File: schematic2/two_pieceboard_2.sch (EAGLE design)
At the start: 17 parts, among them J1 2X5P-2.54, Q1 MOSFET-NCHANNELFDD8580, Q2 MOSFET-NCHANNELFDD8580, Q4 MOSFET-NCHANNELFDD8580, Q5 MOSFET-NCHANNELFDD8580, Q6 MOSFET-NCHANNELFDD8580, Q7 MOSFET-NCHANNELFDD8580, U3 LM317DCY, X1 MKDSN1,5/2-5,08, X2 MKDSN1,5/3-5,08

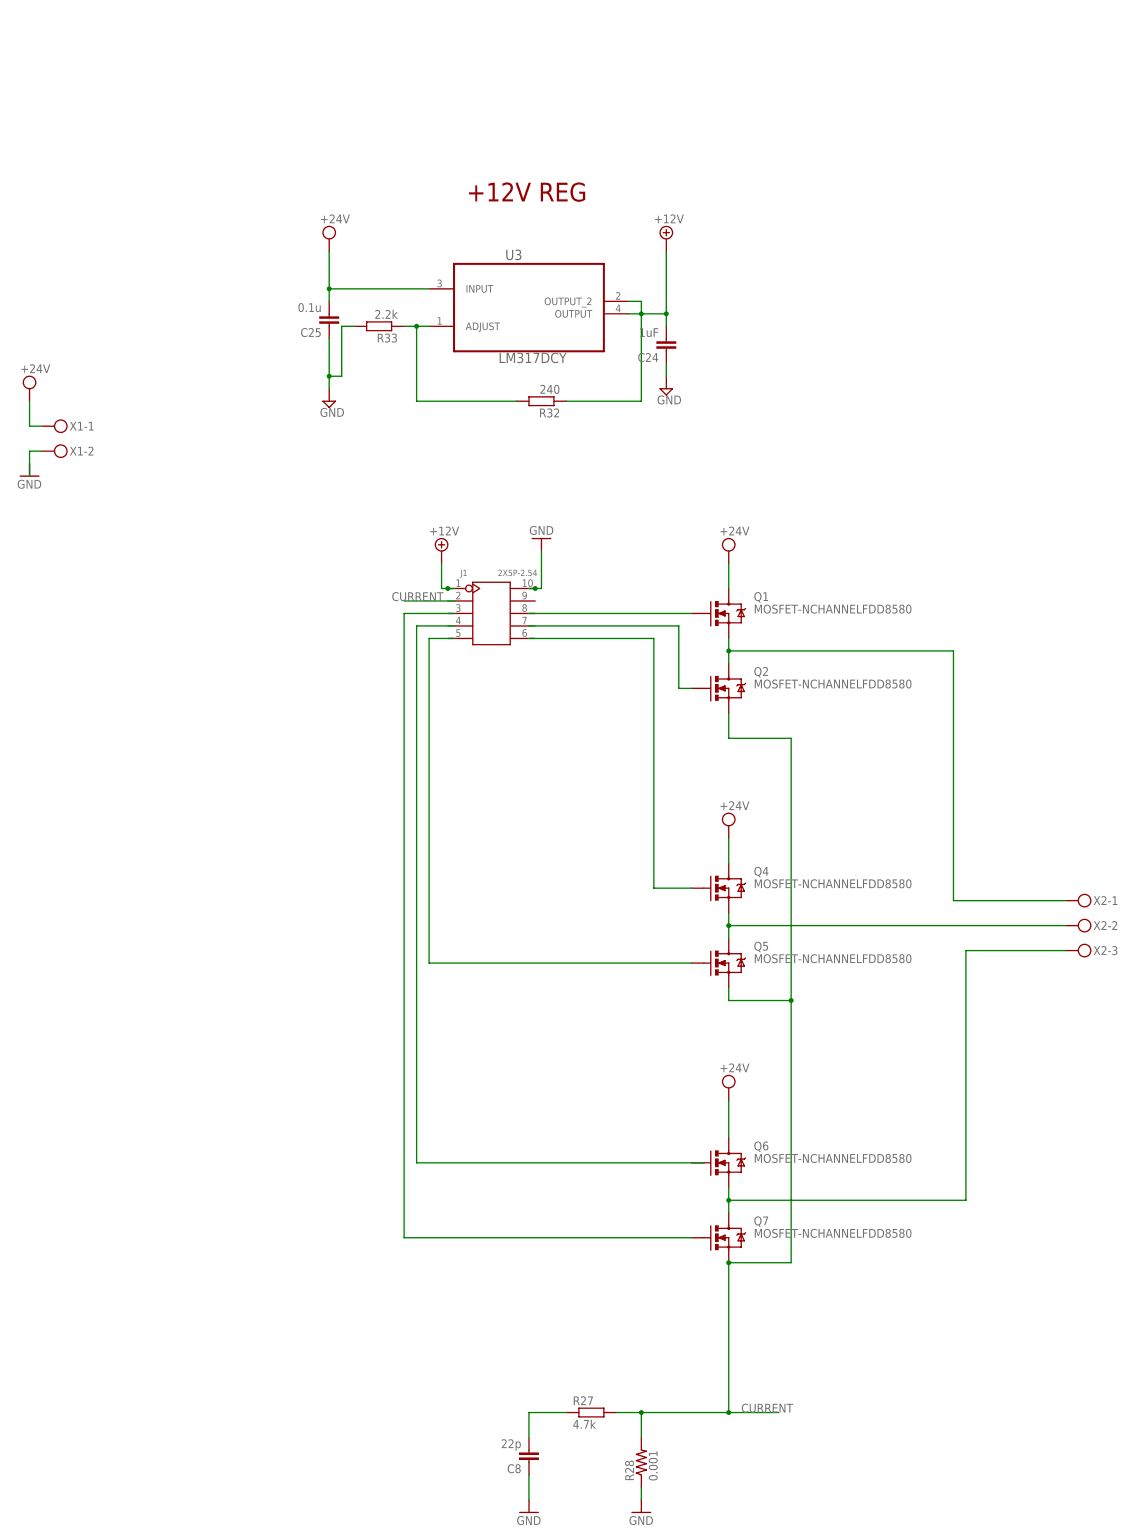
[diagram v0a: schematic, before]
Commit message: finished with FET board generated gerbers.
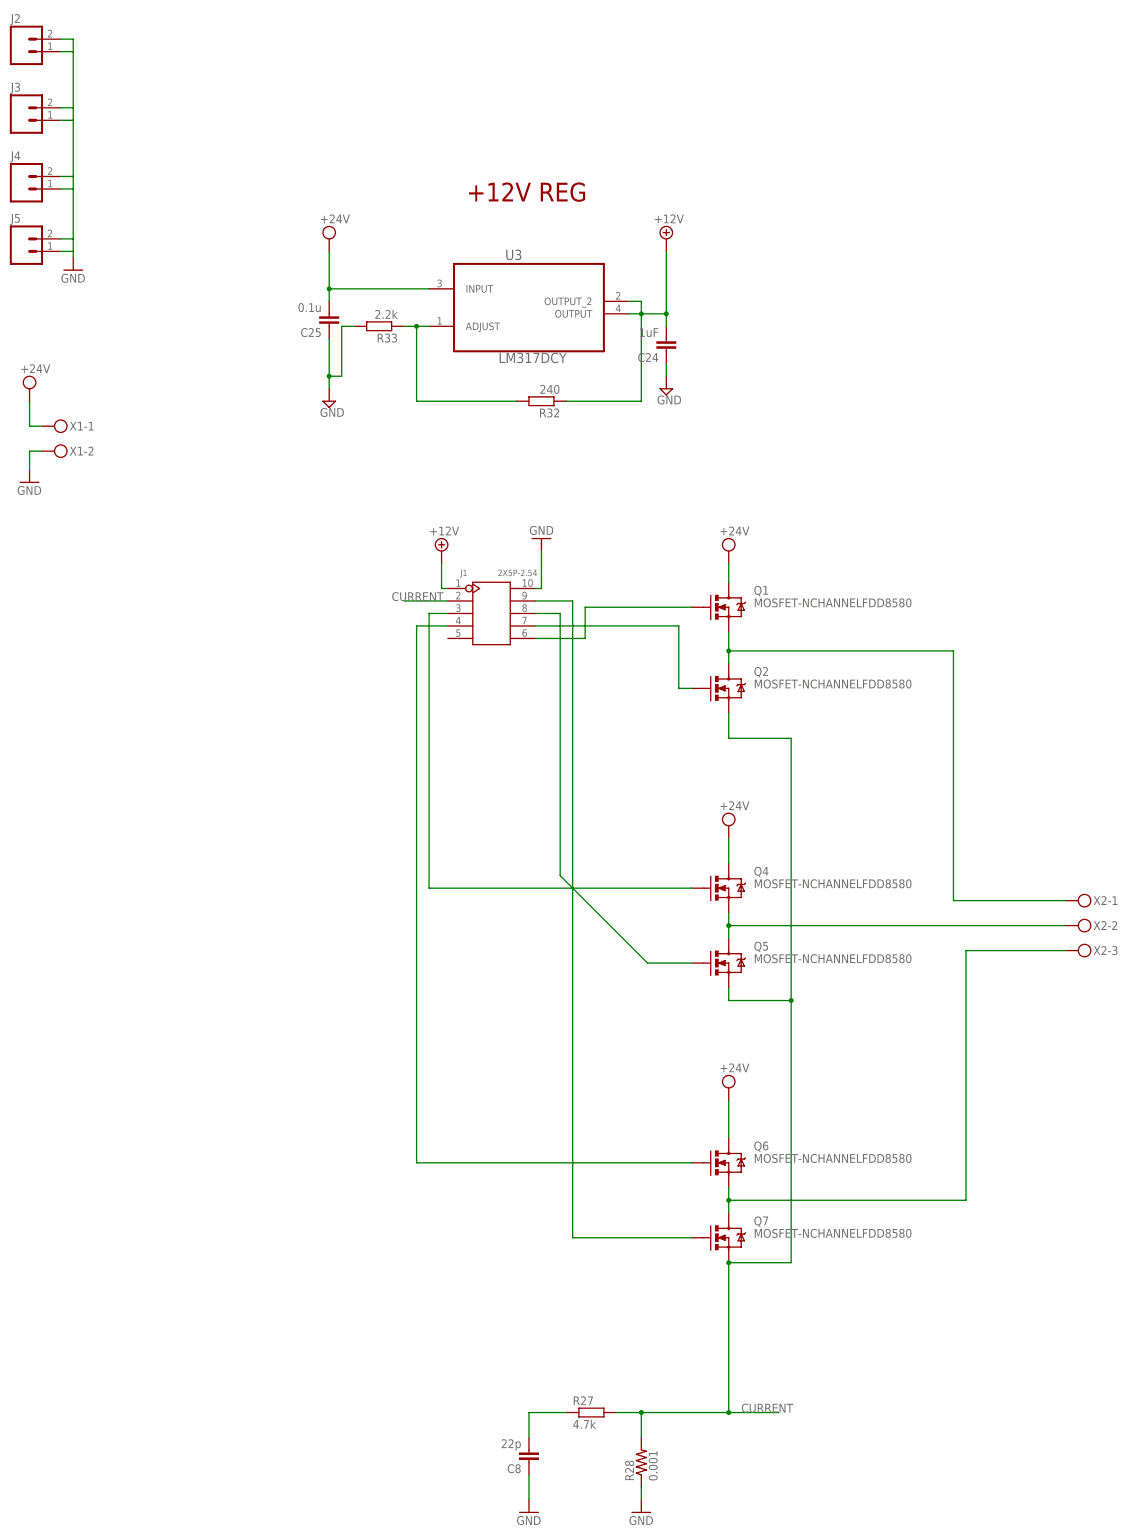
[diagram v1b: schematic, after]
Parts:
- added J2, J3, J4, J5: (no value), SparkFun-Connectors:M02PTH
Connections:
- removed net N$4: Q4.G
- new net N$16: J1.3, Q4.G
- new net N$7: J1.4, Q6.G
- net CURRENT: now also J1.2
- net GND: now also J2.1, J2.2, J3.1, J3.2, J4.1, J4.2, J5.1, J5.2
- net N$1: now also J1.6
- net N$2: now also J1.7
- net N$6: now also J1.8
- net N$8: now also J1.9
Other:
- moved on the sheet: Q1

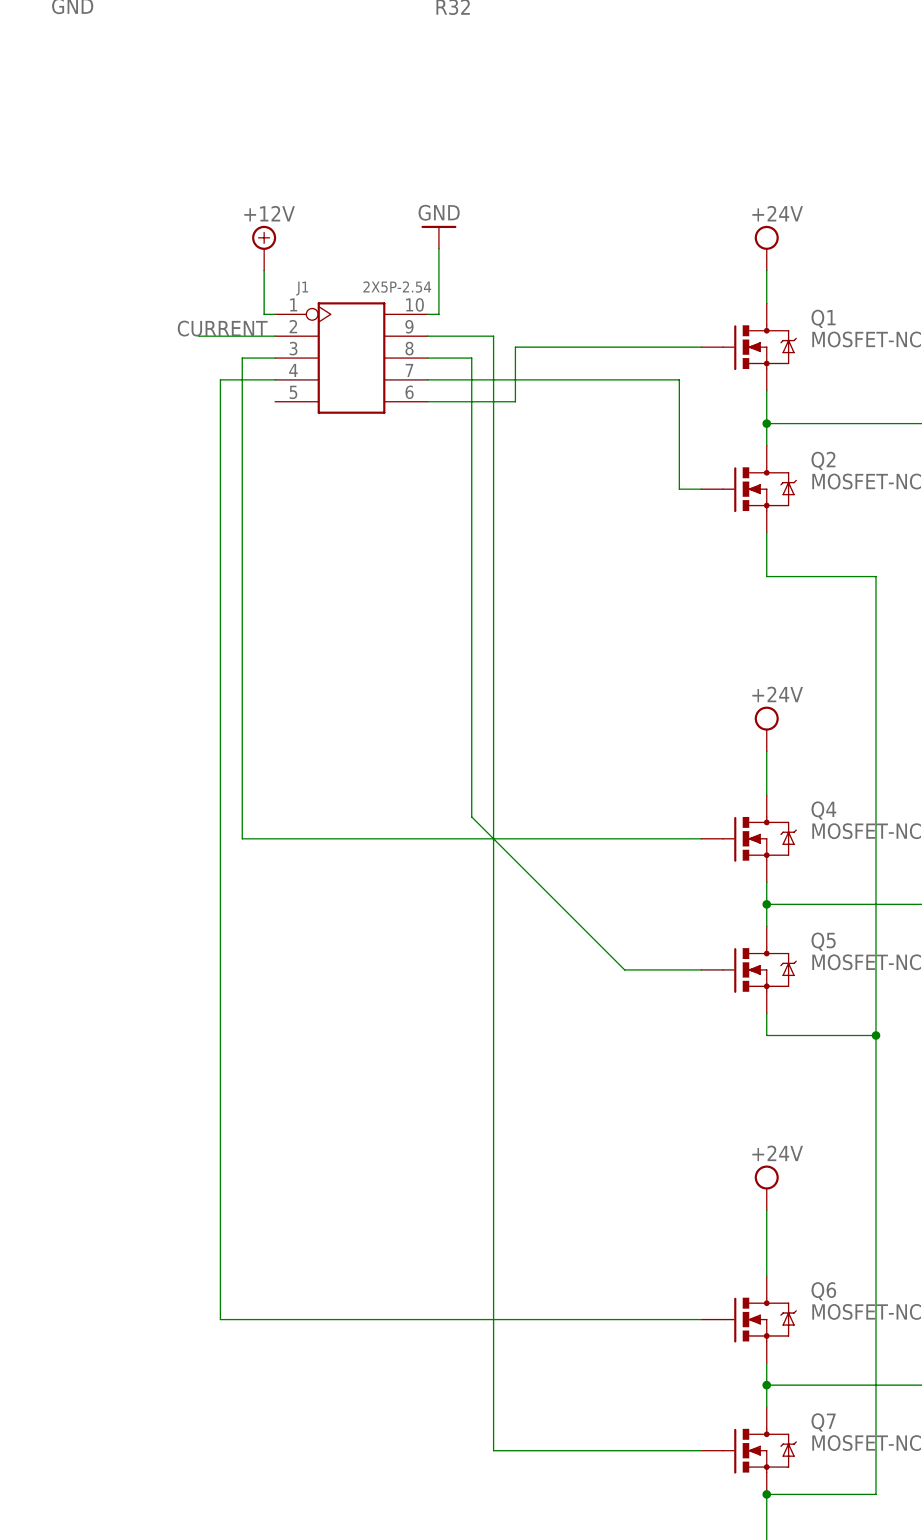
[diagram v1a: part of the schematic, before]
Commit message: added lower line for upper transistor for all three half bridges to connector.
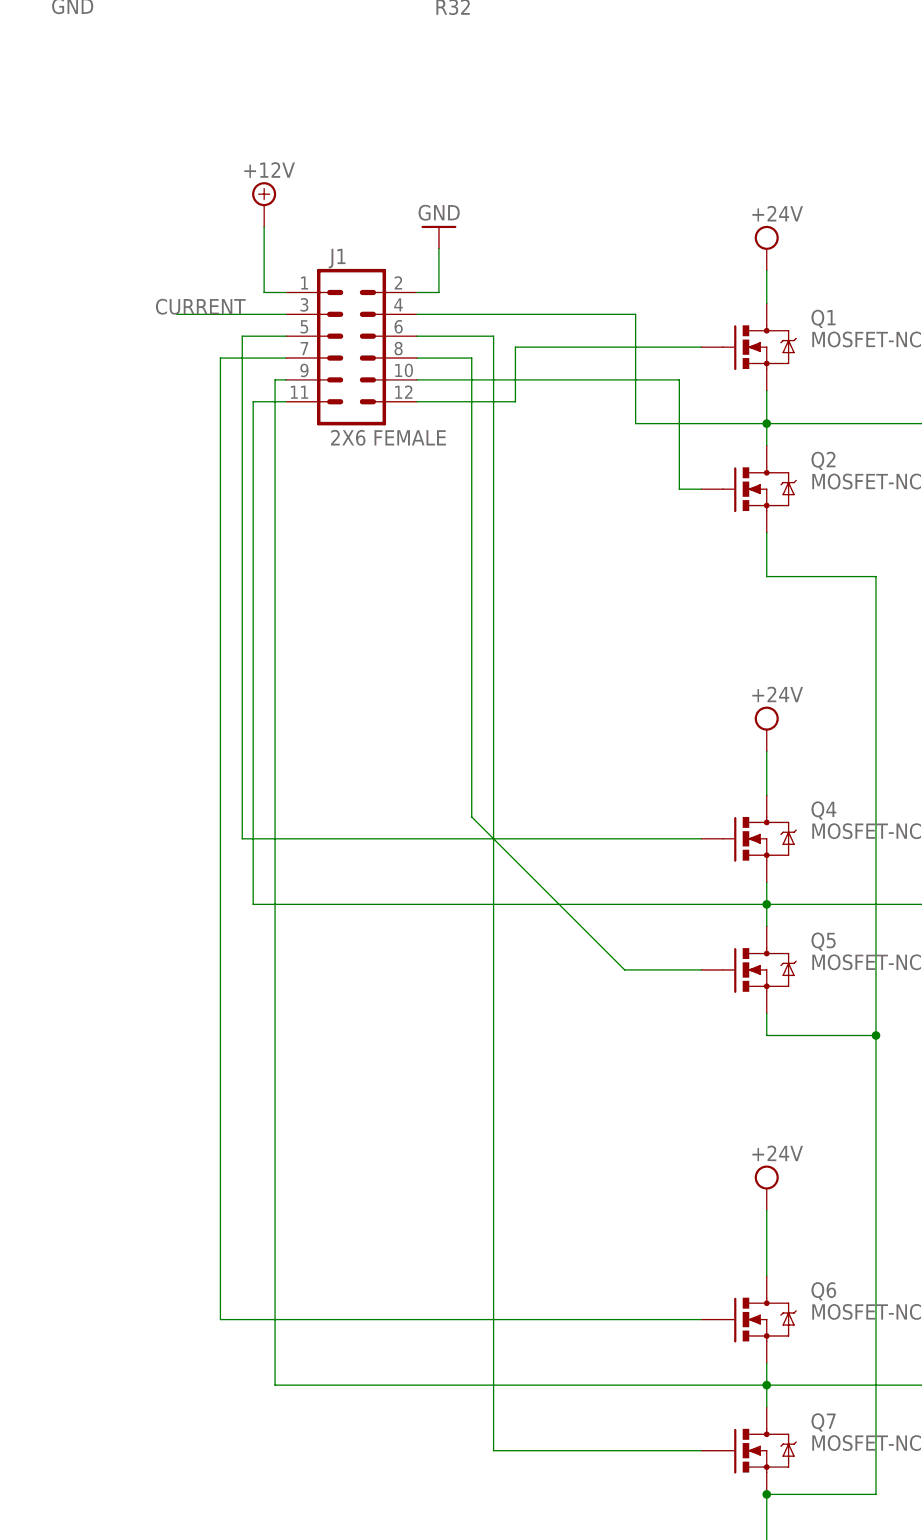
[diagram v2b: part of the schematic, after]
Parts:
- J1: value 2X5P-2.54 -> 2X6 FEMALE; device Seeed-OPL-Connector:DIP-BLACK-FEMALE-HEADER(2X5P-2.54) -> SparkFun-Connectors:M06X2PTH_FEMALE
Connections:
- net BLDC1: now also J1.4
- net BLDC2: now also J1.11
- net BLDC3: now also J1.9
- net CURRENT: now also J1.3; no longer J1.2
- net GND: now also J1.2; no longer J1.10
- net N$1: now also J1.12; no longer J1.6
- net N$16: now also J1.5; no longer J1.3
- net N$2: now also J1.10; no longer J1.7
- net N$7: now also J1.7; no longer J1.4
- net N$8: now also J1.6; no longer J1.9
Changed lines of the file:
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@@
 <part name="C25" library="SmartPrj" deviceset="C-EU" device="C1206" value="0.1u"/>
 <part name="R33" library="SmartPrj" deviceset="R-EU_" device="R1206" value="2.2k"/>
-<part name="J1" library="Seeed-OPL-Connector" deviceset="DIP-BLACK-FEMALE-HEADER(2X5P-2.54)" device="" value="2X5P-2.54"/>
 <part name="GND1" library="supply1" deviceset="GND" device=""/>
 <part name="SUPPLY1" library="supply2" deviceset="+12V" device=""/>
@@
 <part name="J5" library="SparkFun-Connectors" deviceset="M02" device="PTH"/>
 <part name="GND3" library="supply1" deviceset="GND" device=""/>
+<part name="J1" library="SparkFun-Connectors" deviceset="M06X2" device="PTH_FEMALE" value="2X6 FEMALE"/>
 </parts>
 <sheets>
@@
 <instance part="C25" gate="G$1" x="-55.88" y="177.8" rot="R180"/>
 <instance part="R33" gate="G$1" x="-45.72" y="177.8" rot="R180"/>
-<instance part="J1" gate="G$1" x="-22.86" y="119.38"/>
 <instance part="GND1" gate="1" x="-12.7" y="134.62" rot="R180"/>
-<instance part="SUPPLY1" gate="+12V" x="-33.02" y="132.08"/>
+<instance part="SUPPLY1" gate="+12V" x="-33.02" y="137.16"/>
 <instance part="J2" gate="G$1" x="-118.11" y="233.68"/>
 <instance part="J3" gate="G$1" x="-118.11" y="219.71"/>
@@
 <instance part="J5" gate="G$1" x="-118.11" y="193.04"/>
 <instance part="GND3" gate="1" x="-107.95" y="189.23"/>
+<instance part="J1" gate="G$1" x="-25.4" y="114.3"/>
 </instances>
 <busses>
@@
 <pinref part="X2" gate="-1" pin="KL"/>
 <junction x="25.4" y="111.76"/>
+<pinref part="J1" gate="G$1" pin="4"/>
+<wire x1="-15.24" y1="124.46" x2="10.16" y2="124.46" width="0.1524" layer="91"/>
+<wire x1="10.16" y1="124.46" x2="10.16" y2="111.76" width="0.1524" layer="91"/>
+<wire x1="10.16" y1="111.76" x2="25.4" y2="111.76" width="0.1524" layer="91"/>
 </segment>
 </net>
@@
 <wire x1="25.4" y1="55.88" x2="93.98" y2="55.88" width="0.1524" layer="91"/>
 <junction x="25.4" y="55.88"/>
+<pinref part="J1" gate="G$1" pin="11"/>
+<wire x1="-30.48" y1="114.3" x2="-34.29" y2="114.3" width="0.1524" layer="91"/>
+<wire x1="-34.29" y1="114.3" x2="-34.29" y2="55.88" width="0.1524" layer="91"/>
+<wire x1="-34.29" y1="55.88" x2="25.4" y2="55.88" width="0.1524" layer="91"/>
 </segment>
 </net>
@@
 <wire x1="73.66" y1="50.8" x2="93.98" y2="50.8" width="0.1524" layer="91"/>
 <pinref part="X2" gate="-3" pin="KL"/>
+<pinref part="J1" gate="G$1" pin="9"/>
+<wire x1="-30.48" y1="116.84" x2="-31.75" y2="116.84" width="0.1524" layer="91"/>
+<wire x1="-31.75" y1="116.84" x2="-31.75" y2="0" width="0.1524" layer="91"/>
+<wire x1="-31.75" y1="0" x2="25.4" y2="0" width="0.1524" layer="91"/>
 </segment>
 </net>
@@
 </segment>
 <segment>
-<wire x1="-31.75" y1="121.92" x2="-40.64" y2="121.92" width="0.1524" layer="91"/>
-<label x="-43.18" y="121.92" size="1.778" layer="95"/>
-<pinref part="J1" gate="G$1" pin="2"/>
+<label x="-45.72" y="124.46" size="1.778" layer="95"/>
+<pinref part="J1" gate="G$1" pin="3"/>
+<wire x1="-30.48" y1="124.46" x2="-43.18" y2="124.46" width="0.1524" layer="91"/>
 </segment>
 </net>
@@
 <wire x1="12.7" y1="170.18" x2="12.7" y2="167.64" width="0.1524" layer="91"/>
 <pinref part="C24" gate="G$1" pin="1"/>
-</segment>
-<segment>
-<pinref part="GND1" gate="1" pin="GND"/>
-<wire x1="-12.7" y1="132.08" x2="-12.7" y2="124.46" width="0.1524" layer="91"/>
-<wire x1="-12.7" y1="124.46" x2="-13.97" y2="124.46" width="0.1524" layer="91"/>
-<pinref part="J1" gate="G$1" pin="10"/>
 </segment>
 <segment>
@@
 <wire x1="-110.49" y1="233.68" x2="-107.95" y2="233.68" width="0.1524" layer="91"/>
 </segment>
+<segment>
+<pinref part="J1" gate="G$1" pin="2"/>
+<wire x1="-15.24" y1="127" x2="-12.7" y2="127" width="0.1524" layer="91"/>
+<pinref part="GND1" gate="1" pin="GND"/>
+<wire x1="-12.7" y1="127" x2="-12.7" y2="132.08" width="0.1524" layer="91"/>
+</segment>
 </net>
 <net name="N$5" class="0">
@@
 </segment>
 <segment>
-<wire x1="-33.02" y1="129.54" x2="-33.02" y2="124.46" width="0.1524" layer="91"/>
-<wire x1="-33.02" y1="124.46" x2="-31.75" y2="124.46" width="0.1524" layer="91"/>
+<wire x1="-33.02" y1="134.62" x2="-33.02" y2="127" width="0.1524" layer="91"/>
+<pinref part="SUPPLY1" gate="+12V" pin="+12V"/>
 <pinref part="J1" gate="G$1" pin="1"/>
-<pinref part="SUPPLY1" gate="+12V" pin="+12V"/>
+<wire x1="-33.02" y1="127" x2="-30.48" y2="127" width="0.1524" layer="91"/>
 </segment>
 </net>
@@
 <wire x1="17.78" y1="104.14" x2="15.24" y2="104.14" width="0.1524" layer="91"/>
 <wire x1="15.24" y1="104.14" x2="15.24" y2="116.84" width="0.1524" layer="91"/>
+<pinref part="J1" gate="G$1" pin="10"/>
+<wire x1="15.24" y1="116.84" x2="-15.24" y2="116.84" width="0.1524" layer="91"/>
+</segment>
+</net>
+<net name="N$7" class="0">
+<segment>
+<wire x1="17.78" y1="7.62" x2="-38.1" y2="7.62" width="0.1524" layer="91"/>
+<wire x1="-38.1" y1="7.62" x2="-38.1" y2="119.38" width="0.1524" layer="91"/>
+<pinref part="Q6" gate="G$1" pin="G"/>
 <pinref part="J1" gate="G$1" pin="7"/>
-<wire x1="15.24" y1="116.84" x2="-13.97" y2="116.84" width="0.1524" layer="91"/>
-</segment>
-</net>
-<net name="N$7" class="0">
-<segment>
-<wire x1="17.78" y1="7.62" x2="-38.1" y2="7.62" width="0.1524" layer="91"/>
-<wire x1="-38.1" y1="7.62" x2="-38.1" y2="116.84" width="0.1524" layer="91"/>
-<pinref part="Q6" gate="G$1" pin="G"/>
-<pinref part="J1" gate="G$1" pin="4"/>
-<wire x1="-31.75" y1="116.84" x2="-38.1" y2="116.84" width="0.1524" layer="91"/>
+<wire x1="-30.48" y1="119.38" x2="-38.1" y2="119.38" width="0.1524" layer="91"/>
 </segment>
 </net>
@@
 <wire x1="17.78" y1="-7.62" x2="-6.35" y2="-7.62" width="0.1524" layer="91"/>
 <wire x1="-6.35" y1="-7.62" x2="-6.35" y2="121.92" width="0.1524" layer="91"/>
-<pinref part="J1" gate="G$1" pin="9"/>
-<wire x1="-6.35" y1="121.92" x2="-13.97" y2="121.92" width="0.1524" layer="91"/>
+<pinref part="J1" gate="G$1" pin="6"/>
+<wire x1="-6.35" y1="121.92" x2="-15.24" y2="121.92" width="0.1524" layer="91"/>
 </segment>
 </net>
 <net name="N$1" class="0">
 <segment>
-<pinref part="J1" gate="G$1" pin="6"/>
-<wire x1="-13.97" y1="114.3" x2="-3.81" y2="114.3" width="0.1524" layer="91"/>
 <wire x1="-3.81" y1="114.3" x2="-3.81" y2="120.65" width="0.1524" layer="91"/>
 <pinref part="Q1" gate="G$1" pin="G"/>
 <wire x1="-3.81" y1="120.65" x2="17.78" y2="120.65" width="0.1524" layer="91"/>
+<pinref part="J1" gate="G$1" pin="12"/>
+<wire x1="-3.81" y1="114.3" x2="-15.24" y2="114.3" width="0.1524" layer="91"/>
 </segment>
 </net>
@@
 <wire x1="8.89" y1="48.26" x2="17.78" y2="48.26" width="0.1524" layer="91"/>
 <pinref part="J1" gate="G$1" pin="8"/>
-<wire x1="-8.89" y1="119.38" x2="-13.97" y2="119.38" width="0.1524" layer="91"/>
+<wire x1="-8.89" y1="119.38" x2="-15.24" y2="119.38" width="0.1524" layer="91"/>
 </segment>
 </net>
@@
 <pinref part="Q4" gate="G$1" pin="G"/>
 <wire x1="17.78" y1="63.5" x2="-35.56" y2="63.5" width="0.1524" layer="91"/>
-<wire x1="-35.56" y1="63.5" x2="-35.56" y2="119.38" width="0.1524" layer="91"/>
-<pinref part="J1" gate="G$1" pin="3"/>
-<wire x1="-35.56" y1="119.38" x2="-31.75" y2="119.38" width="0.1524" layer="91"/>
-</segment>
-</net>
+<wire x1="-35.56" y1="63.5" x2="-35.56" y2="121.92" width="0.1524" layer="91"/>
+<pinref part="J1" gate="G$1" pin="5"/>
+<wire x1="-35.56" y1="121.92" x2="-30.48" y2="121.92" width="0.1524" layer="91"/>
+</segment>
+</net>
